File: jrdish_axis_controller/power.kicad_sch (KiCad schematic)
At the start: 23 parts, among them CN6 KF2EDGR-2.54-2P, Q1 AO3407A, SW2 SS-12F49-G050, U4 MP2322GQH-Z

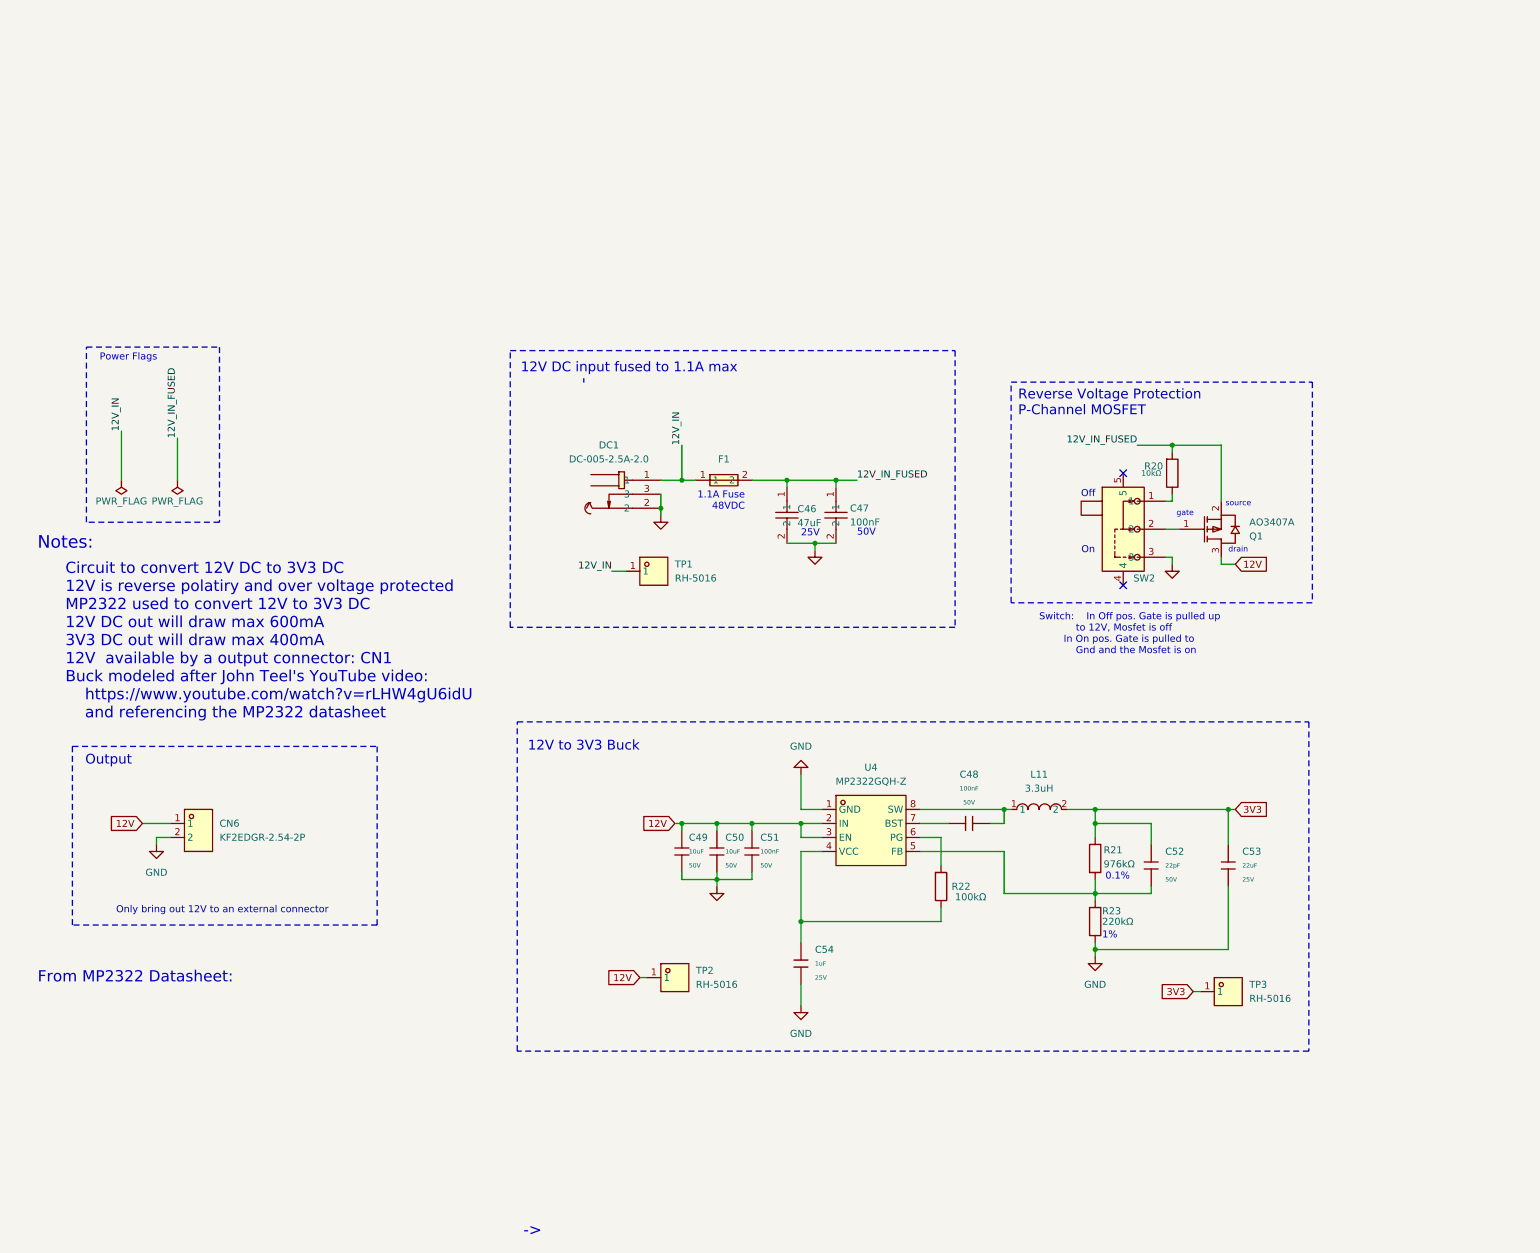
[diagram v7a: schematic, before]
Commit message: Limit switches with mosfets
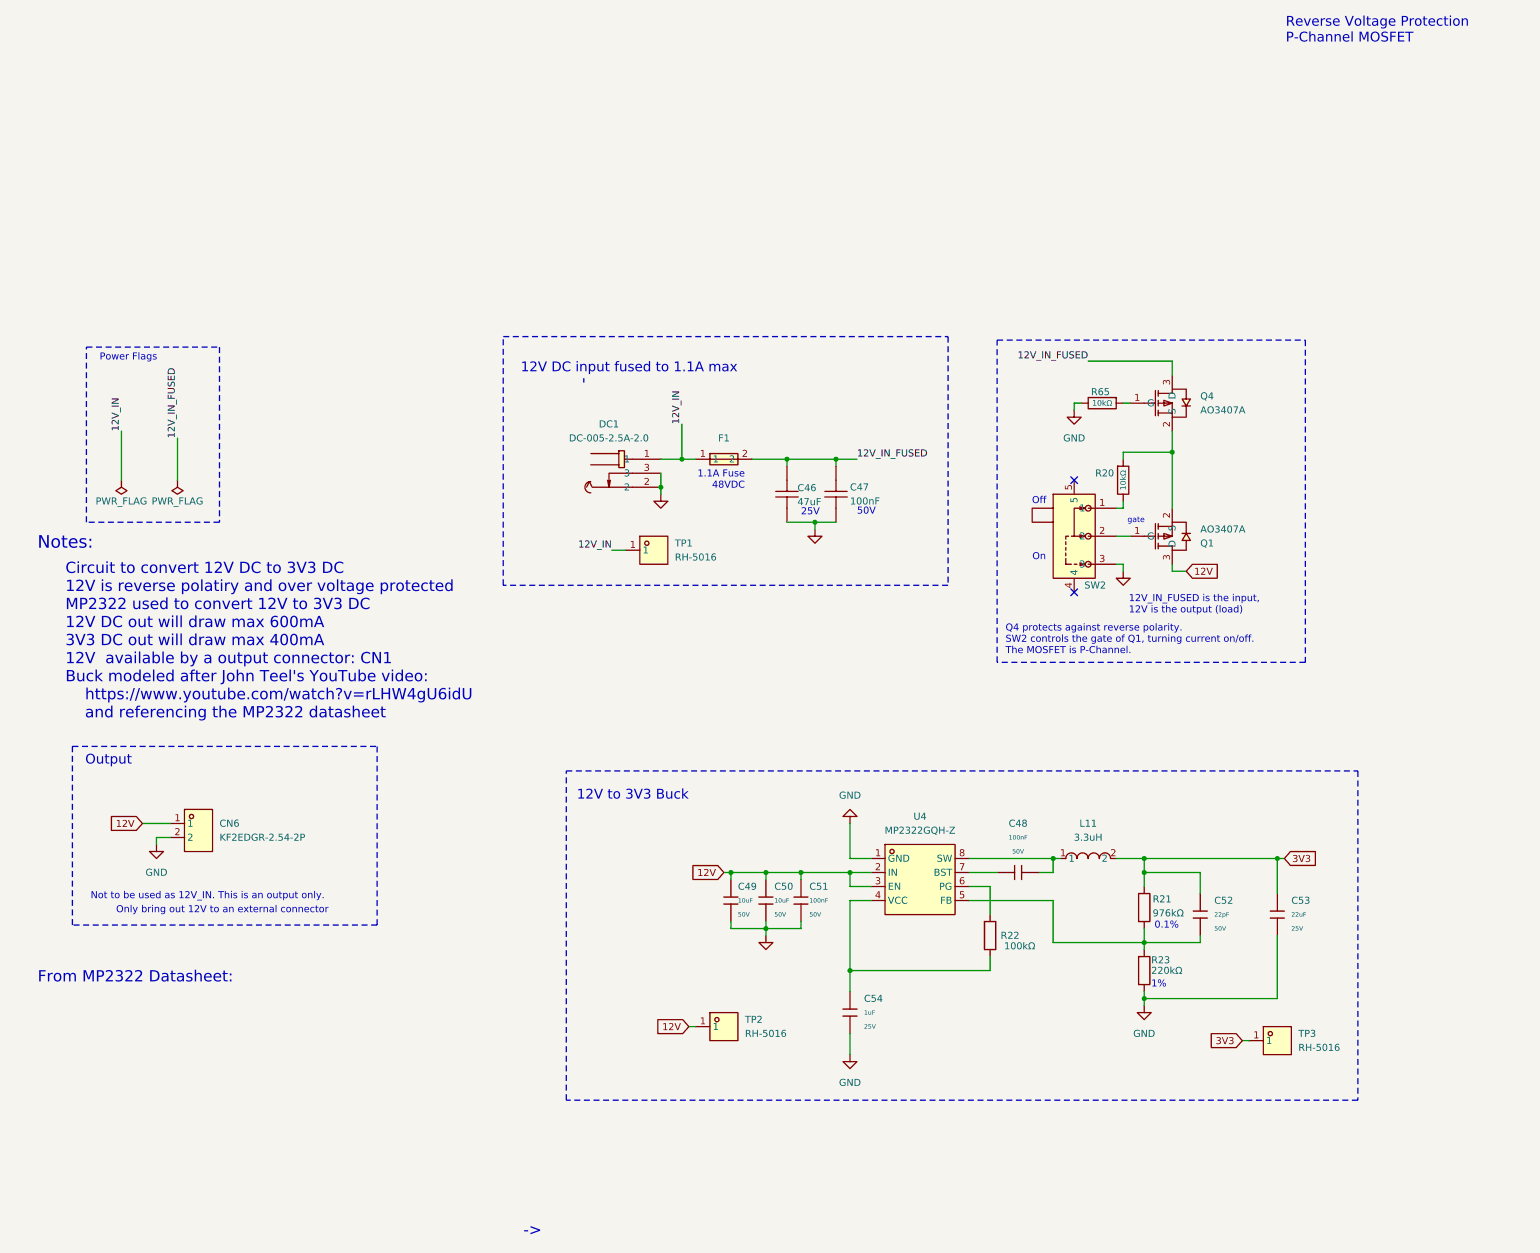
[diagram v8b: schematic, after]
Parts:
- added Q4: AO3407A, MyParts:SOT-23-3_L2.9-W1.6-P1.90-LS2.8-BR, symbol MyParts:AO3407A
- added R65: 10kΩ, PCM_JLCPCB:R_0603, symbol PCM_JLCPCB-Resistors:0603,10kΩ
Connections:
- net 12V_IN_FUSED: now also Q4.3 (D); no longer Q1.2 (S), R20.1
- net GND: now reaches C46.2, C47.2
- net GND: now also C49.2, C50.2, C51.2, C53.2, C54.2, CN6.2, DC1.2, DC1.3, R23.2, SW2.3, U4.1 (GND), R65.2
- new net: Q1.2 (S), Q4.2 (S), R20.1
- new net: Q4.1 (G), R65.1
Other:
- note added: "12V_IN_FUSED is the input, 12V is the output (load)"
- note added: "Not to be used as 12V_IN. This is an output only."
- note added: "Q4 protects against reverse polarity. SW2 controls the gate of Q1, turning current on/off. The MOSFET is P-Channel."
- note removed: "Switch: In Off pos. Gate is pulled up to 12V, Mosfet is off In On pos. Gate is pulled to Gnd and the Mosfet is on"
- note removed: "drain"
- note removed: "source"
- moved on the sheet: C48, C49, C50, C51, C52, C53, C54, DC1, F1, L11, R20, R21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
